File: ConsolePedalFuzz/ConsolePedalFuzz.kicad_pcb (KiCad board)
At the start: 2 copper layers, 100 x 60 mm, 18 parts, among them J1 Conn_02x25_Counter_Clockwise, Q1 2N3904, Q2 2N3904

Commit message: Made polarized capacitors axial so lid could fit. Replotted gerber files
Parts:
- C1: footprint Capacitor_THT:CP_Radial_D5.0mm_P2.50mm -> Capacitor_THT:CP_Axial_L11.0mm_D5.0mm_P18.00mm_Horizontal
- C3: footprint Capacitor_THT:CP_Radial_D6.3mm_P2.50mm -> Capacitor_THT:CP_Axial_L11.0mm_D6.0mm_P18.00mm_Horizontal
- moved C1 34.5 mm to (165.0, 91.2), turned to 270 degrees
- moved C3 32.9 mm to (100.5, 91.2), turned to 270 degrees
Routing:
- net Net-(C3-Pad1): track 39.4 -> 62.4 mm
- net /Input: track 97.0 -> 86.5 mm, vias 3 -> 2
- net Net-(C1-Pad1): track 27.1 -> 35.9 mm
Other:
- board text added: "Console Pedal Fuzz V1.1"
- board text removed: "Console Pedal Fuzz V1.0"

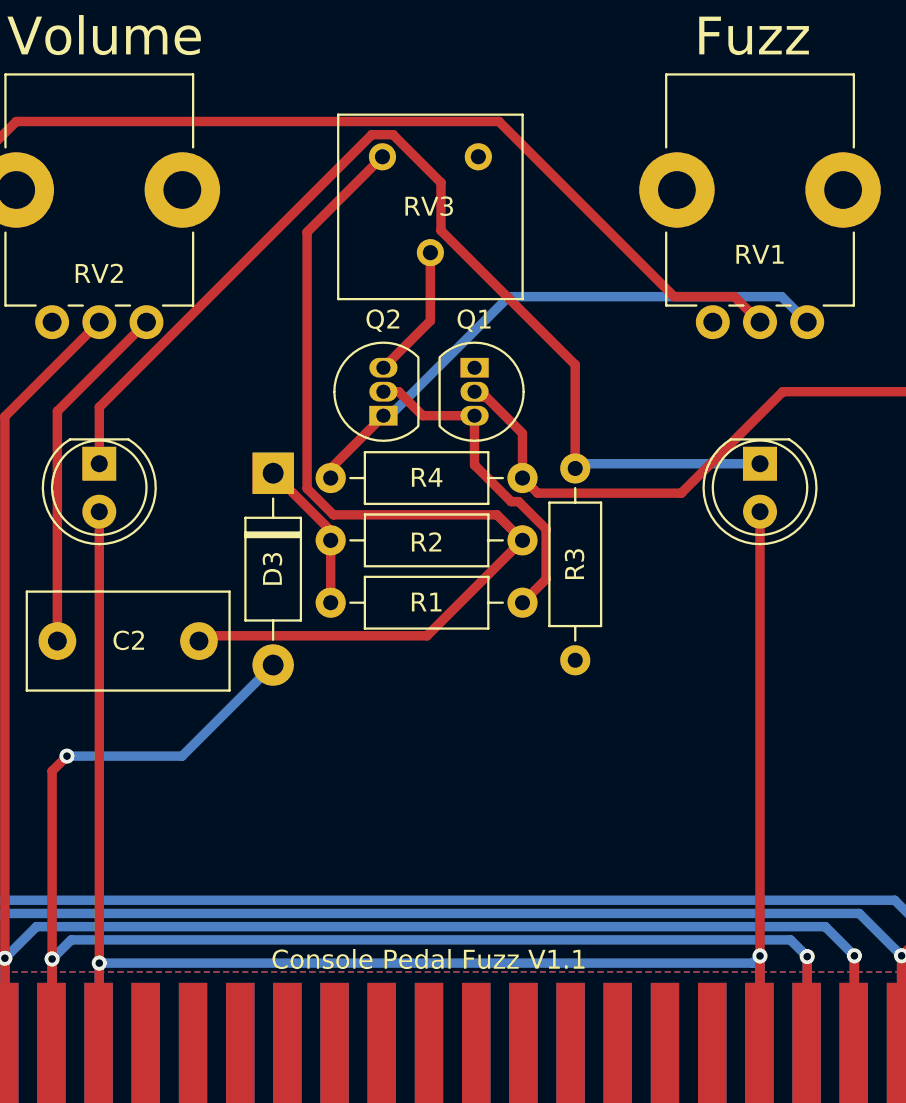
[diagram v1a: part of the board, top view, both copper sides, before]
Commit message: Added jlcpcb order number location
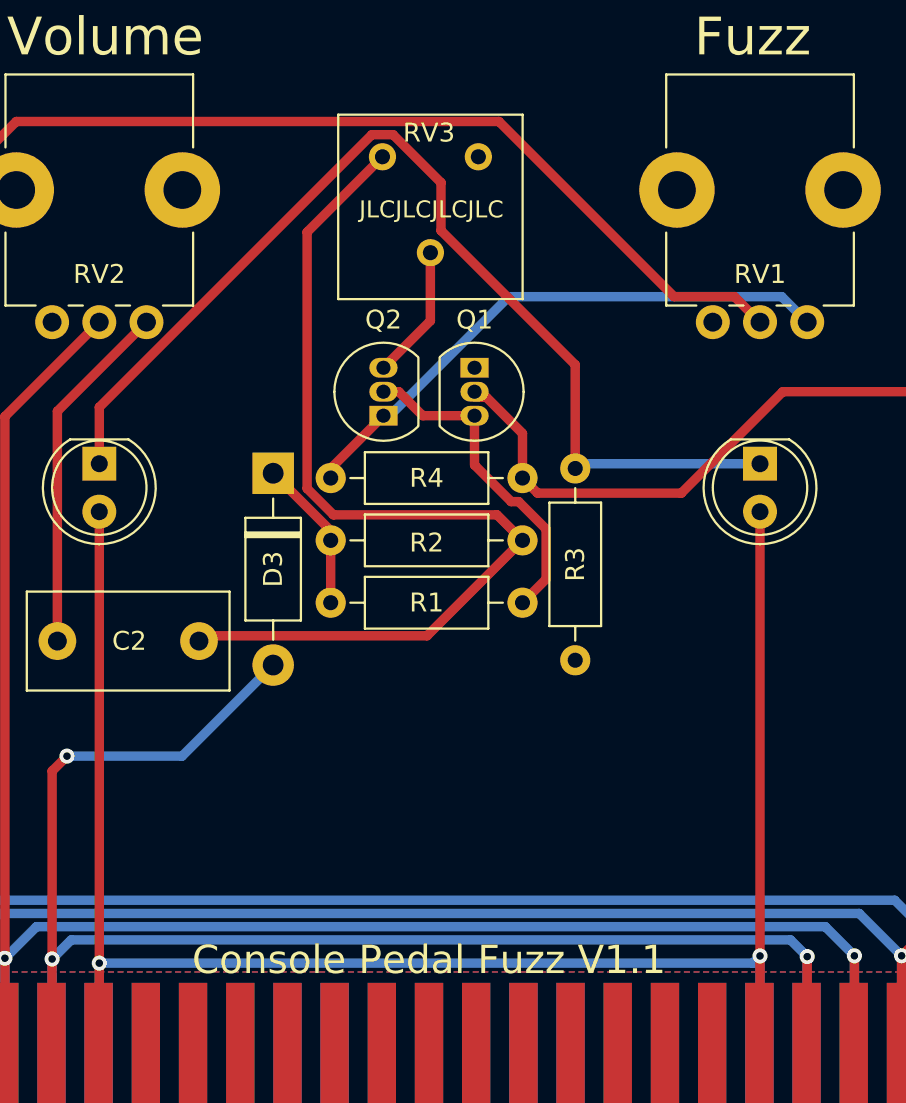
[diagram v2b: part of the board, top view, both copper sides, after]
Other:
- board text added: "JLCJLCJLCJLC"

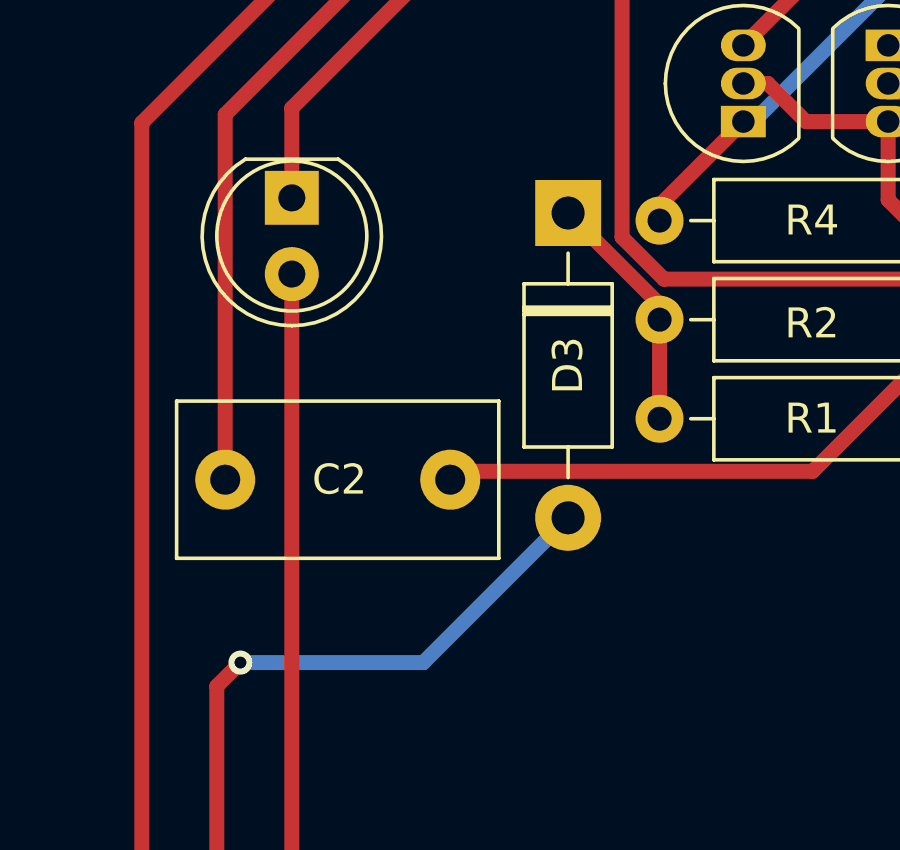
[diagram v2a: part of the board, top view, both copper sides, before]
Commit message: Removed reverse polarity protection diode since mainboard has it now
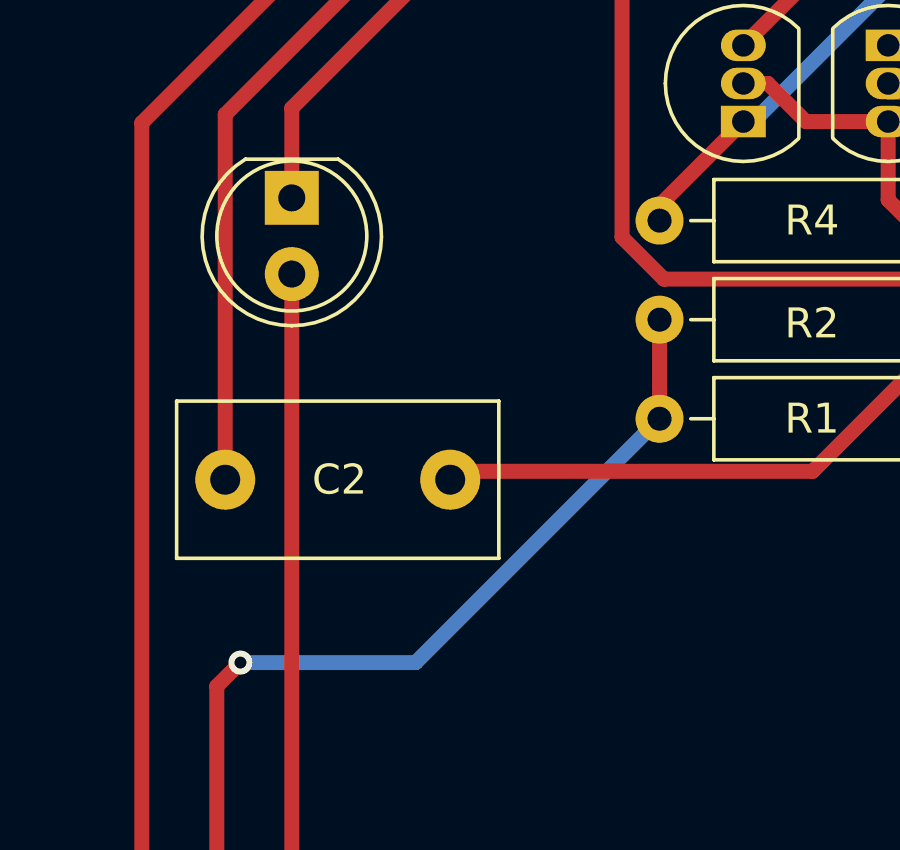
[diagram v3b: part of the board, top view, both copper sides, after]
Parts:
- removed D3: D, Diode_THT:D_DO-41_SOD81_P10.16mm_Horizontal
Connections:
- R1 pad 2: Net-(D3-Pad1) -> +9V
- R2 pad 2: Net-(D3-Pad1) -> +9V
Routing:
- net +9V: track 84.1 -> 92.3 mm
- net Net-(D3-Pad1): track 8.12 -> 0.00 mm

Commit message: Fixed footprints and replotted
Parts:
- C2: footprint Capacitor_THT:C_Disc_D10.5mm_W5.0mm_P7.50mm -> libraries:C_Flat_L7.2_H6.5
- J1: footprint libraries:N64-Connector -> libraries:N64-Connector-Wide
- moved C2 2.30 mm to (112.8, 102.1)
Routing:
- net Net-(C2-Pad2): track 51.1 -> 44.4 mm
- net Net-(C2-Pad1): track 18.8 -> 16.3 mm
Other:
- outline, holes or cut-outs redrawn
- board text added: "Console Pedal Fuzz V1.2"
- board text added: "Thomas McDonagh consolepedals.com"
- board text removed: "Console Pedal Fuzz V1.1"
- board text removed: "Thomas McDonagh mcdonaghcorp.com"

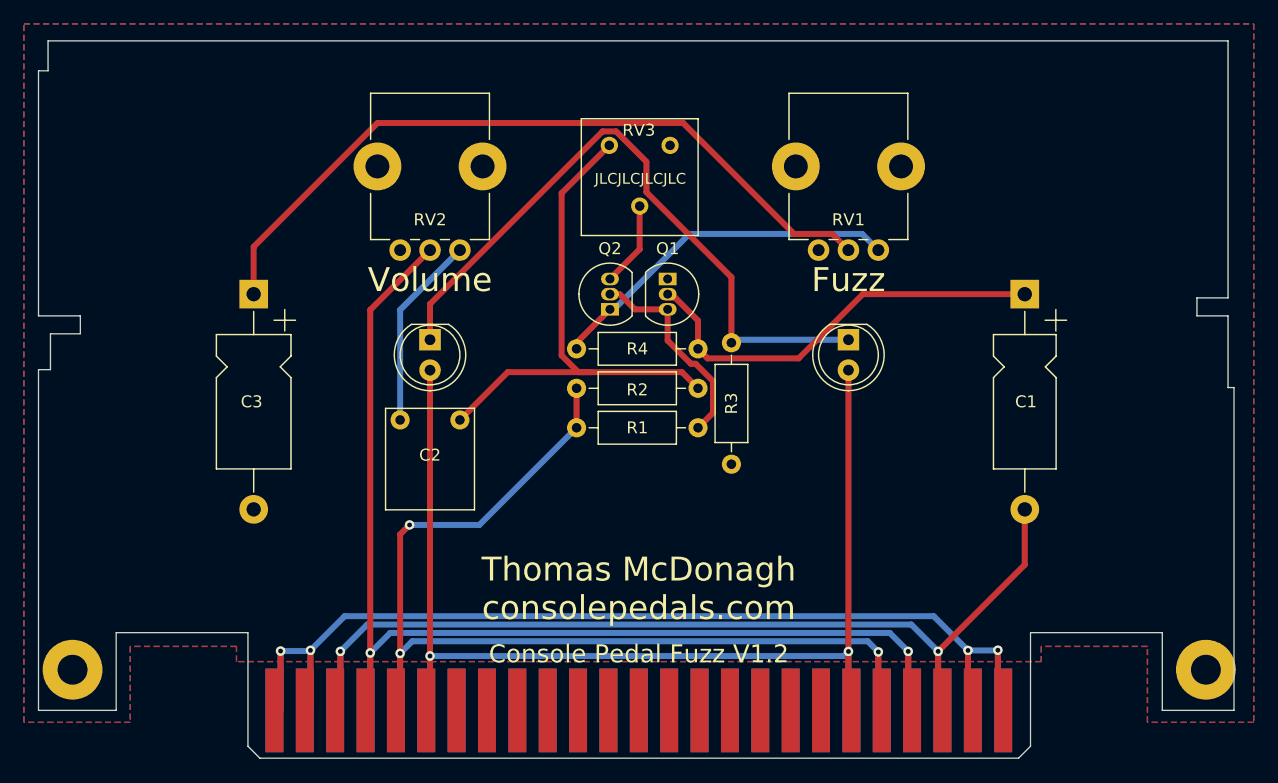
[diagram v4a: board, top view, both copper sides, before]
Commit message: Fixed minor trace issue
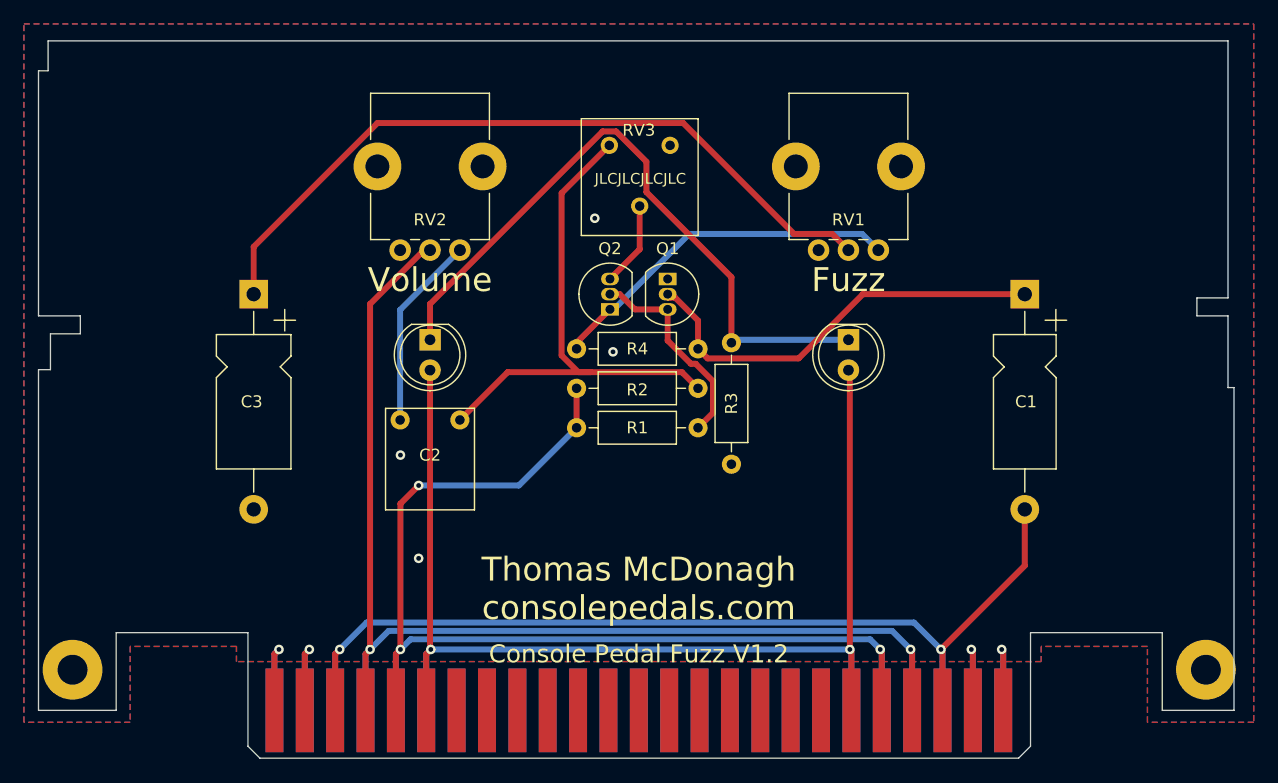
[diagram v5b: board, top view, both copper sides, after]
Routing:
- net GND: track 102.5 -> 41.6 mm, vias 4 -> 8
- net +9V: track 92.3 -> 95.0 mm
- net /Output: track 101.6 -> 103.1 mm
- net /LEDPower: track 101.6 -> 102.7 mm
- net /Input: track 86.5 -> 87.6 mm
